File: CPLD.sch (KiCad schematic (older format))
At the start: 35 parts, among them J5 JTAG, SW2 SW_DIP_x06, SW3 User PB, U12 74HCT3G04, U3 EPM7064STC100, X1 CFPS-72 50mhz

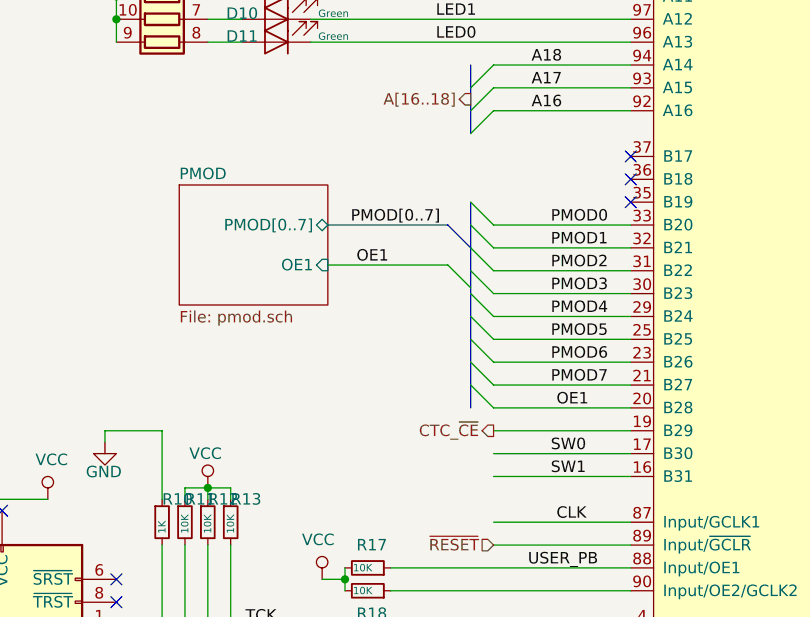
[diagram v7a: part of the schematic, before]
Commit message: fixed pmod pins
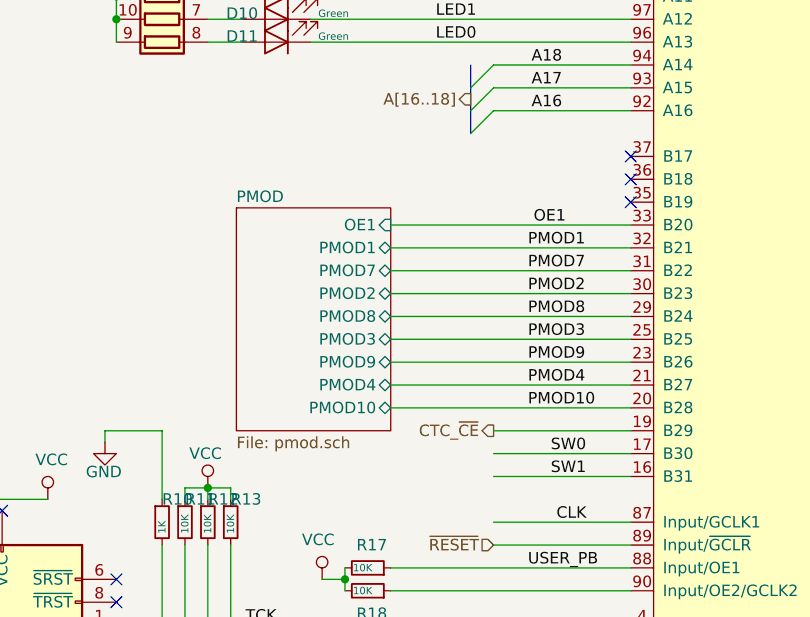
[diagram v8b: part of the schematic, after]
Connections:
- net labels added: PMOD10, PMOD8, PMOD9
- net labels removed: PMOD0, PMOD5, PMOD6, PMOD[0..7]
- wire segments 187 -> 186
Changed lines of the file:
@@
 	6150 1350 6750 1350
 Wire Wire Line
-	6150 3150 6750 3150
-Wire Wire Line
-	6150 3250 6750 3250
-Wire Wire Line
-	6150 3350 6750 3350
-Wire Wire Line
-	6150 3450 6750 3450
-Wire Wire Line
-	6150 3550 6750 3550
-Wire Wire Line
-	6150 3650 6750 3650
-Wire Wire Line
-	6150 3750 6750 3750
-Wire Wire Line
-	6150 3850 6750 3850
+	5700 3150 6750 3150
+Wire Wire Line
+	5700 3250 6750 3250
+Wire Wire Line
+	5700 3350 6750 3350
+Wire Wire Line
+	5700 3450 6750 3450
+Wire Wire Line
+	5700 3550 6750 3550
+Wire Wire Line
+	5700 3650 6750 3650
+Wire Wire Line
+	5700 3750 6750 3750
+Wire Wire Line
+	5700 3850 6750 3850
 Wire Wire Line
 	8950 1850 9550 1850
@@
 Text Label 6350 1550 0    50   ~ 0
 SW5
-Text Label 6400 3150 0    50   ~ 0
-PMOD0
-Text Label 6400 3250 0    50   ~ 0
+Text Label 6300 3250 0    50   ~ 0
 PMOD1
-Text Label 6400 3350 0    50   ~ 0
+Text Label 6300 3450 0    50   ~ 0
 PMOD2
-Text Label 6400 3450 0    50   ~ 0
+Text Label 6300 3650 0    50   ~ 0
 PMOD3
-Text Label 6400 3550 0    50   ~ 0
+Text Label 6300 3850 0    50   ~ 0
 PMOD4
-Text Label 6400 3650 0    50   ~ 0
-PMOD5
-Text Label 6400 3750 0    50   ~ 0
-PMOD6
-Text Label 6400 3850 0    50   ~ 0
+Text Label 6300 3350 0    50   ~ 0
 PMOD7
+Text Label 6300 3550 0    50   ~ 0
+PMOD8
+Text Label 6300 3750 0    50   ~ 0
+PMOD9
 Text Label 9250 2950 0    50   ~ 0
 D0
@@
 Text HLabel 6050 2600 0    50   Output ~ 0
 A[16..18]
-$Sheet
-S 4775 2975 650  525
-U 5DC790D1
-F0 "PMOD" 50
-F1 "pmod.sch" 50
-F2 "PMOD[0..7]" B R 5425 3150 50
-F3 "OE1" I R 5425 3325 50
-$EndSheet
-Wire Bus Line
-	5425 3150 5950 3150
-Text Label 5525 3150 0    50   ~ 0
-PMOD[0..7]
-Wire Wire Line
-	5425 3325 5950 3325
-Text Label 5550 3325 0    50   ~ 0
-OE1
-Wire Wire Line
-	6150 3950 6750 3950
-Text Label 6425 3950 0    50   ~ 0
+Wire Wire Line
+	5700 3950 6750 3950
+Text Label 6325 3150 0    50   ~ 0
 OE1
 NoConn ~ 6750 2950
@@
 Text Label 3450 3450 0    50   ~ 0
 CLK
-Entry Wire Line
-	6050 3050 6150 3150
-Entry Wire Line
-	6050 3150 6150 3250
-Entry Wire Line
-	6050 3250 6150 3350
-Entry Wire Line
-	6050 3350 6150 3450
-Entry Wire Line
-	6050 3450 6150 3550
-Entry Wire Line
-	6050 3550 6150 3650
-Entry Wire Line
-	6050 3650 6150 3750
-Entry Wire Line
-	6050 3750 6150 3850
-Entry Wire Line
-	6050 3850 6150 3950
-Entry Bus Bus
-	5950 3150 6050 3250
-Entry Wire Line
-	5950 3325 6050 3425
 NoConn ~ 6750 3050
 Entry Wire Line
@@
 Wire Wire Line
 	2050 5200 2400 5200
+$Sheet
+S 5025 3075 675  975
+U 5DC790D1
+F0 "PMOD" 50
+F1 "pmod.sch" 50
+F2 "OE1" I R 5700 3150 50
+F3 "PMOD1" T R 5700 3250 50
+F4 "PMOD2" T R 5700 3450 50
+F5 "PMOD3" T R 5700 3650 50
+F6 "PMOD4" T R 5700 3850 50
+F7 "PMOD7" T R 5700 3350 50
+F8 "PMOD8" T R 5700 3550 50
+F9 "PMOD9" T R 5700 3750 50
+F10 "PMOD10" T R 5700 3950 50
+$EndSheet
+Text Label 6300 3950 0    50   ~ 0
+PMOD10
 Wire Bus Line
 	6050 2450 6050 2750
@@
 	9650 2050 9650 2750
 Wire Bus Line
-	6050 3050 6050 3950
-Wire Bus Line
 	9650 2850 9650 3650
